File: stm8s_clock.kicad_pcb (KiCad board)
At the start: 2 copper layers, 200 x 80 mm, 157 parts, among them J1 Conn_01x04, J2 PS, Q1 BC847, Q10 BC847, Q11 BC847, Q12 BC847, Q13 BC847, Q14 BC847, Q15 BC847, Q16 BC847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

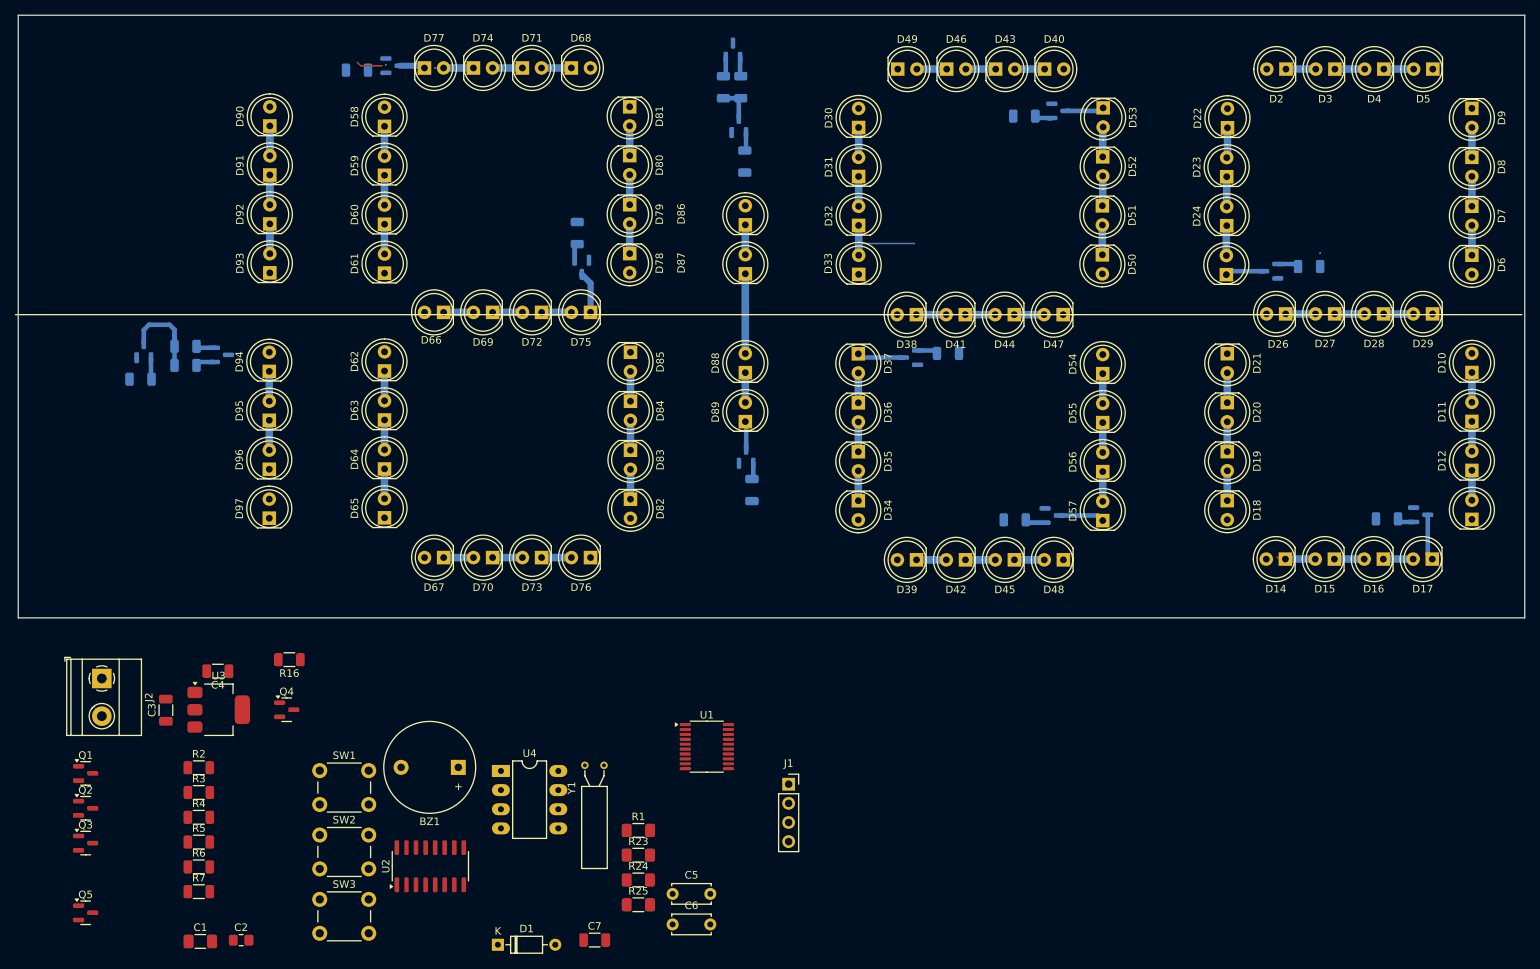
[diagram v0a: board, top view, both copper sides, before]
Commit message: move transistor to workspace
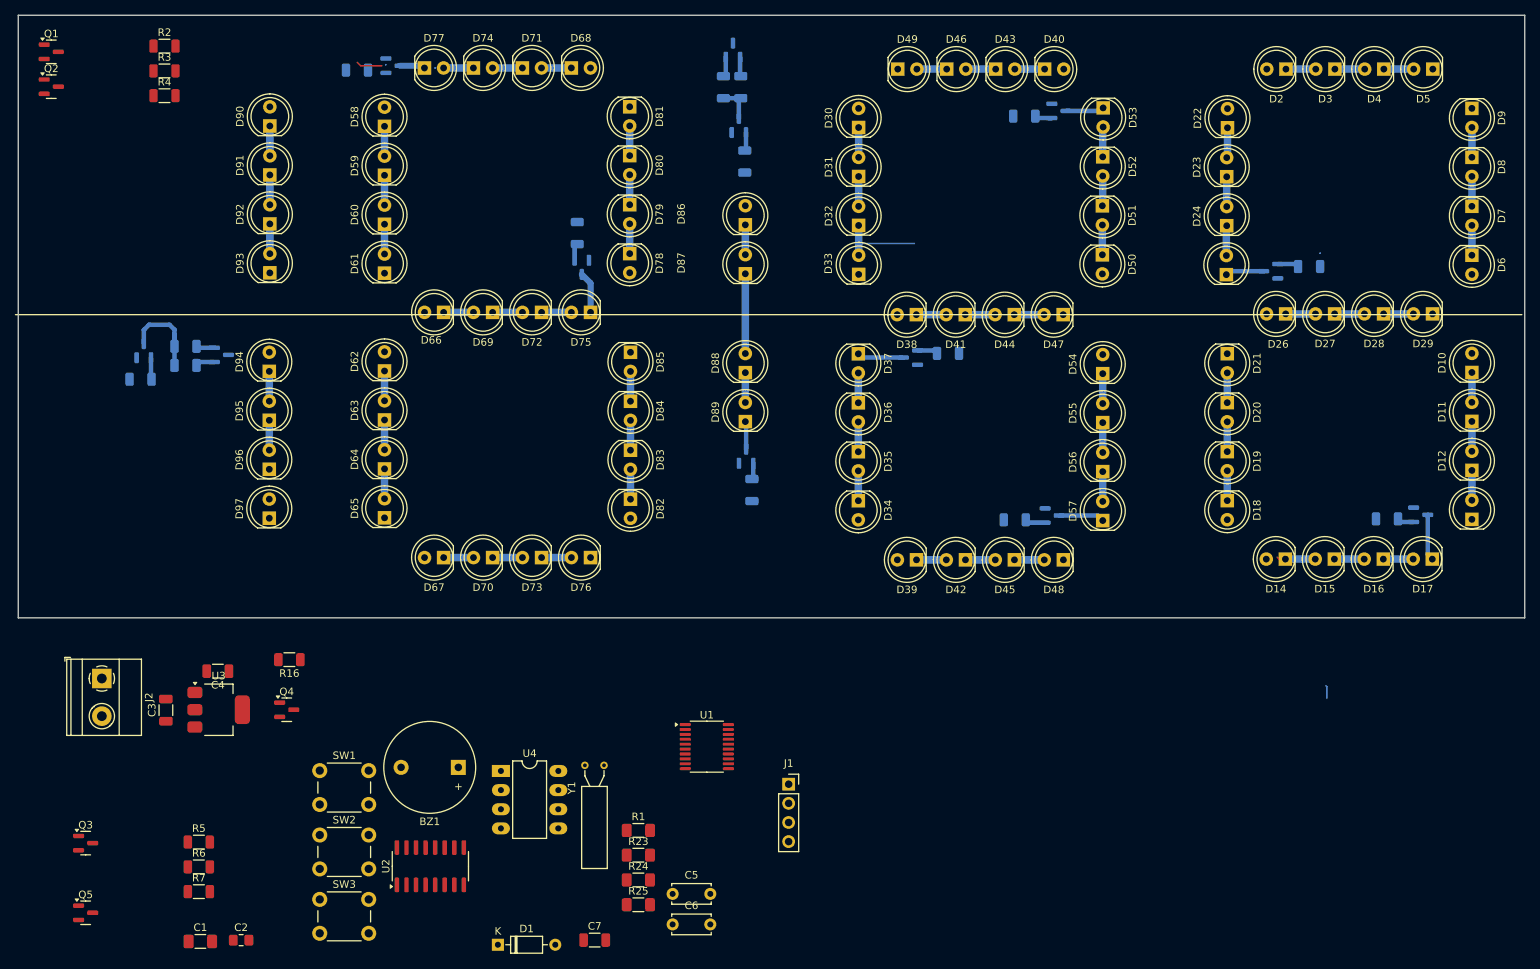
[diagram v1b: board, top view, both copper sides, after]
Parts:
- moved R4 95.9 mm to (82.2, 60.6)
- moved R2 95.9 mm to (82.2, 54.0)
- moved Q1 95.9 mm to (67.2, 54.8)
- moved Q2 95.9 mm to (67.2, 59.4)
- moved R3 95.9 mm to (82.2, 57.3)
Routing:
- net (no net): track 0.00 -> 1.74 mm
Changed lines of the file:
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@@
 	(footprint "Resistor_SMD:R_1206_3216Metric"
 		(layer "F.Cu")
-		(at 86.75 153.14)
+		(at 82.1875 57.34)
 		(descr "Resistor SMD 1206 (3216 Metric), square (rectangular) end terminal, IPC_7351 nominal, (Body size source: IPC-SM-782 page 72, https://www.pcb-3d.com/wordpress/wp-content/uploads/ipc-sm-782a_amendment_1_and_2.pdf), generated with kicad-footprint-generator")
 		(tags "resistor")
@@
 	(footprint "Package_TO_SOT_SMD:SOT-23"
 		(layer "F.Cu")
-		(at 71.72 150.605)
+		(at 67.1575 54.805)
 		(descr "SOT, 3 Pin (https://www.jedec.org/system/files/docs/to-236h.pdf variant AB), generated with kicad-footprint-generator ipc_gullwing_generator.py")
 		(tags "SOT TO_SOT_SMD")
@@
 	(footprint "Package_TO_SOT_SMD:SOT-23"
 		(layer "F.Cu")
-		(at 71.72 155.23)
+		(at 67.1575 59.43)
 		(descr "SOT, 3 Pin (https://www.jedec.org/system/files/docs/to-236h.pdf variant AB), generated with kicad-footprint-generator ipc_gullwing_generator.py")
 		(tags "SOT TO_SOT_SMD")
@@
 	(footprint "Resistor_SMD:R_1206_3216Metric"
 		(layer "F.Cu")
-		(at 86.75 156.43)
+		(at 82.1875 60.63)
 		(descr "Resistor SMD 1206 (3216 Metric), square (rectangular) end terminal, IPC_7351 nominal, (Body size source: IPC-SM-782 page 72, https://www.pcb-3d.com/wordpress/wp-content/uploads/ipc-sm-782a_amendment_1_and_2.pdf), generated with kicad-footprint-generator")
 		(tags "resistor")
@@
 		)
 		(property "Value" "LED"
-			(at 1.19 3.96 -0)
+			(at 1.19 3.96 0)
 			(layer "B.Fab")
 			(effects
@@
 	(footprint "Resistor_SMD:R_1206_3216Metric"
 		(layer "F.Cu")
-		(at 86.75 149.85)
+		(at 82.1875 54.05)
 		(descr "Resistor SMD 1206 (3216 Metric), square (rectangular) end terminal, IPC_7351 nominal, (Body size source: IPC-SM-782 page 72, https://www.pcb-3d.com/wordpress/wp-content/uploads/ipc-sm-782a_amendment_1_and_2.pdf), generated with kicad-footprint-generator")
 		(tags "resistor")
@@
 		(tags "SOT TO_SOT_SMD")
 		(property "Reference" "Q11"
-			(at 0 2.4 360)
+			(at 0 2.4 0)
 			(layer "B.SilkS")
 			(effects
@@
 		)
 		(property "Value" "BC847"
-			(at 0 -2.4 360)
+			(at 0 -2.4 0)
 			(layer "B.Fab")
 			(effects
@@
 		)
 		(fp_text user "${REFERENCE}"
-			(at 0 0 360)
+			(at 0 0 0)
 			(layer "B.Fab")
 			(effects
@@
 		(tags "resistor")
 		(property "Reference" "R13"
-			(at 0 1.82 360)
+			(at 0 1.82 0)
 			(layer "B.SilkS")
 			(effects
@@
 		)
 		(property "Value" "470R"
-			(at 0 -1.82 360)
+			(at 0 -1.82 0)
 			(layer "B.Fab")
 			(effects
@@
 		)
 		(fp_text user "${REFERENCE}"
-			(at 0 0 360)
+			(at 0 0 0)
 			(layer "B.Fab")
 			(effects
@@
 		(tags "SOT TO_SOT_SMD")
 		(property "Reference" "Q12"
-			(at 0 2.4 360)
+			(at 0 2.4 0)
 			(layer "B.SilkS")
 			(effects
@@
 		)
 		(property "Value" "BC847"
-			(at 0 -2.4 360)
+			(at 0 -2.4 0)
 			(layer "B.Fab")
 			(effects
@@
 		)
 		(fp_text user "${REFERENCE}"
-			(at 0 0 360)
+			(at 0 0 0)
 			(layer "B.Fab")
 			(effects
@@
 		(tags "SOT TO_SOT_SMD")
 		(property "Reference" "Q10"
-			(at 0 2.4 360)
+			(at 0 2.4 0)
 			(layer "B.SilkS")
 			(effects
@@
 		)
 		(property "Value" "BC847"
-			(at 0 -2.4 360)
+			(at 0 -2.4 0)
 			(layer "B.Fab")
 			(effects
@@
 		)
 		(fp_text user "${REFERENCE}"
-			(at 3.51 9.235 360)
+			(at 3.51 9.235 0)
 			(layer "B.Fab")
 			(effects
@@
 		(tags "SOT TO_SOT_SMD")
 		(property "Reference" "Q9"
-			(at 0 2.4 360)
+			(at 0 2.4 0)
 			(layer "B.SilkS")
 			(effects
@@
 		)
 		(property "Value" "BC857"
-			(at 0 -2.4 360)
+			(at 0 -2.4 0)
 			(layer "B.Fab")
 			(effects
@@
 		)
 		(fp_text user "${REFERENCE}"
-			(at 0 0 360)
+			(at 0 0 0)
 			(layer "B.Fab")
 			(effects
@@
 		(tags "SOT TO_SOT_SMD")
 		(property "Reference" "Q13"
-			(at 0 2.4 360)
+			(at 0 2.4 0)
 			(layer "B.SilkS")
 			(effects
@@
 		)
 		(property "Value" "BC847"
-			(at 0 -2.4 360)
+			(at 0 -2.4 0)
 			(layer "B.Fab")
 			(effects
@@
 		)
 		(fp_text user "${REFERENCE}"
-			(at 0 0 360)
+			(at 0 0 0)
 			(layer "B.Fab")
 			(effects
@@
 		(tags "resistor")
 		(property "Reference" "R11"
-			(at 0 1.82 360)
+			(at 0 1.82 0)
 			(layer "B.SilkS")
 			(effects
@@
 		)
 		(property "Value" "4.7k"
-			(at 0 -1.82 360)
+			(at 0 -1.82 0)
 			(layer "B.Fab")
 			(effects
@@
 		)
 		(fp_text user "${REFERENCE}"
-			(at 0 0 360)
+			(at 0 0 0)
 			(layer "B.Fab")
 			(effects
@@
 		(tags "SOT TO_SOT_SMD")
 		(property "Reference" "Q15"
-			(at 0 2.4 360)
+			(at 0 2.4 0)
 			(layer "B.SilkS")
 			(effects
@@
 		)
 		(property "Value" "BC847"
-			(at 0 -2.4 360)
+			(at 0 -2.4 0)
 			(layer "B.Fab")
 			(effects
@@
 		)
 		(fp_text user "${REFERENCE}"
-			(at 0 0 360)
+			(at 0 0 0)
 			(layer "B.Fab")
 			(effects
@@
 		(tags "resistor")
 		(property "Reference" "R19"
-			(at 0 1.82 360)
+			(at 0 1.82 0)
 			(layer "B.SilkS")
 			(effects
@@
 		)
 		(property "Value" "1k"
-			(at 0 -1.82 360)
+			(at 0 -1.82 0)
 			(layer "B.Fab")
 			(effects
@@
 		)
 		(fp_text user "${REFERENCE}"
-			(at 0 0 360)
+			(at 0 0 0)
 			(layer "B.Fab")
 			(effects
@@
 		(tags "resistor")
 		(property "Reference" "R14"
-			(at 0 1.82 360)
+			(at 0 1.82 0)
 			(layer "B.SilkS")
 			(effects
@@
 		)
 		(property "Value" "1k"
-			(at 0 -1.82 360)
+			(at 0 -1.82 0)
 			(layer "B.Fab")
 			(effects
@@
 		)
 		(fp_text user "${REFERENCE}"
-			(at 0 0 360)
+			(at 0 0 0)
 			(layer "B.Fab")
 			(effects
@@
 		(tags "resistor")
 		(property "Reference" "R15"
-			(at 0 1.82 360)
+			(at 0 1.82 0)
 			(layer "B.SilkS")
 			(effects
@@
 		)
 		(property "Value" "470R"
-			(at 0 -1.82 360)
+			(at 0 -1.82 0)
 			(layer "B.Fab")
 			(effects
@@
 		)
 		(fp_text user "${REFERENCE}"
-			(at 0 0 360)
+			(at 0 0 0)
 			(layer "B.Fab")
 			(effects
@@
 		(tags "resistor")
 		(property "Reference" "R20"
-			(at 0 1.82 360)
+			(at 0 1.82 0)
 			(layer "B.SilkS")
 			(effects
@@
 		)
 		(property "Value" "1k"
-			(at 0 -1.82 360)
+			(at 0 -1.82 0)
 			(layer "B.Fab")
 			(effects
@@
 		)
 		(fp_text user "${REFERENCE}"
-			(at 0 0 360)
+			(at 0 0 0)
 			(layer "B.Fab")
 			(effects
@@
 		(tags "resistor")
 		(property "Reference" "R12"
-			(at 0 1.82 360)
+			(at 0 1.82 0)
 			(layer "B.SilkS")
 			(effects
@@
 		)
 		(property "Value" "4.7k"
-			(at 0 -1.82 360)
+			(at 0 -1.82 0)
 			(layer "B.Fab")
 			(effects
@@
 		)
 		(fp_text user "${REFERENCE}"
-			(at 0 0 360)
+			(at 0 0 0)
 			(layer "B.Fab")
 			(effects
@@
 		(tags "resistor")
 		(property "Reference" "R18"
-			(at 0 1.82 360)
+			(at 0 1.82 0)
 			(layer "B.SilkS")
 			(effects
@@
 		)
 		(property "Value" "1k"
-			(at 0 -1.82 360)
+			(at 0 -1.82 0)
 			(layer "B.Fab")
 			(effects
@@
 		)
 		(fp_text user "${REFERENCE}"
-			(at 0 0 360)
+			(at 0 0 0)
 			(layer "B.Fab")
 			(effects
@@
 		(tags "resistor")
 		(property "Reference" "R17"
-			(at 0 1.82 360)
+			(at 0 1.82 0)
 			(layer "B.SilkS")
 			(effects
@@
 		)
 		(property "Value" "1k"
-			(at 0 -1.82 360)
+			(at 0 -1.82 0)
 			(layer "B.Fab")
 			(effects
@@
 		)
 		(fp_text user "${REFERENCE}"
-			(at 0 0 360)
+			(at 0 0 0)
 			(layer "B.Fab")
 			(effects
@@
 		(tags "SOT TO_SOT_SMD")
 		(property "Reference" "Q14"
-			(at 0 2.4 360)
+			(at 0 2.4 0)
 			(layer "B.SilkS")
 			(effects
@@
 		)
 		(property "Value" "BC847"
-			(at 0 -2.4 360)
+			(at 0 -2.4 0)
 			(layer "B.Fab")
 			(effects
@@
 		)
 		(fp_text user "${REFERENCE}"
-			(at 0 0 360)
+			(at 0 0 0)
 			(layer "B.Fab")
 			(effects
@@
 	)
 	(segment
+		(start 236.5 140.65)
+		(end 236.5 139.09)
+		(width 0.2)
+		(layer "B.Cu")
+		(net 0)
+	)
+	(segment
+		(start 236.5 139.09)
+		(end 236.37 138.96)
+		(width 0.2)
+		(layer "B.Cu")
+		(net 0)
+	)
+	(segment

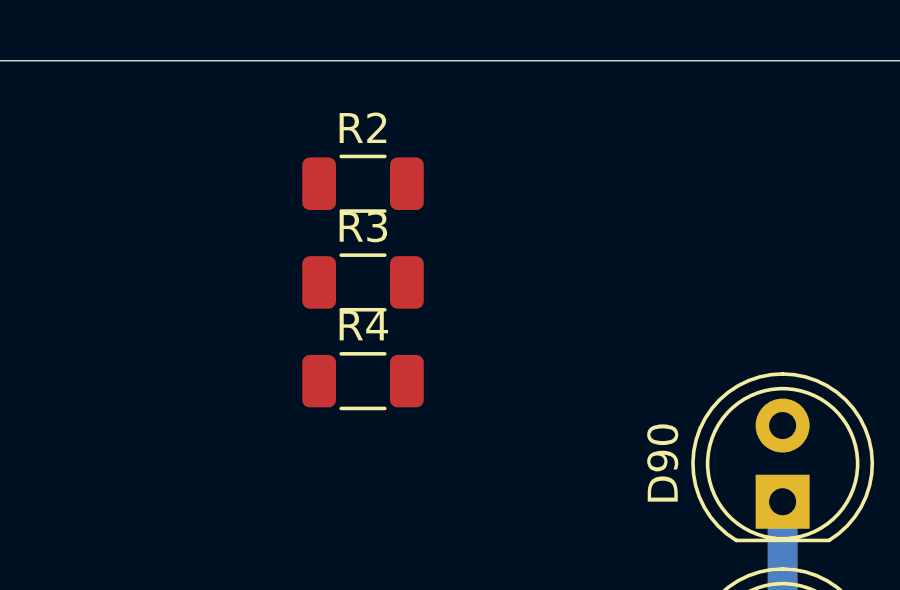
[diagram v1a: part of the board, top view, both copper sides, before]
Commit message: component position changes
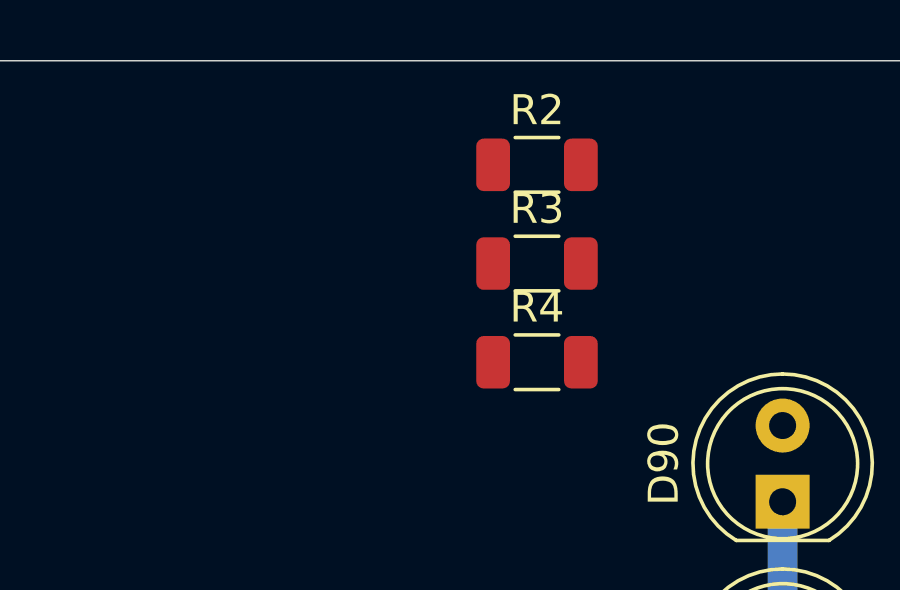
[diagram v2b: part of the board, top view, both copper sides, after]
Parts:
- moved R3 5.83 mm to (88.0, 56.7)
- moved R4 5.83 mm to (88.0, 60.0)
- moved R2 5.83 mm to (88.0, 53.4)
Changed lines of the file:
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@@
 	(footprint "Resistor_SMD:R_1206_3216Metric"
 		(layer "F.Cu")
-		(at 82.1875 57.34)
+		(at 87.9875 56.71)
 		(descr "Resistor SMD 1206 (3216 Metric), square (rectangular) end terminal, IPC_7351 nominal, (Body size source: IPC-SM-782 page 72, https://www.pcb-3d.com/wordpress/wp-content/uploads/ipc-sm-782a_amendment_1_and_2.pdf), generated with kicad-footprint-generator")
 		(tags "resistor")
@@
 	(footprint "Resistor_SMD:R_1206_3216Metric"
 		(layer "F.Cu")
-		(at 82.1875 60.63)
+		(at 87.9875 60)
 		(descr "Resistor SMD 1206 (3216 Metric), square (rectangular) end terminal, IPC_7351 nominal, (Body size source: IPC-SM-782 page 72, https://www.pcb-3d.com/wordpress/wp-content/uploads/ipc-sm-782a_amendment_1_and_2.pdf), generated with kicad-footprint-generator")
 		(tags "resistor")
@@
 	(footprint "Resistor_SMD:R_1206_3216Metric"
 		(layer "F.Cu")
-		(at 82.1875 54.05)
+		(at 87.9875 53.42)
 		(descr "Resistor SMD 1206 (3216 Metric), square (rectangular) end terminal, IPC_7351 nominal, (Body size source: IPC-SM-782 page 72, https://www.pcb-3d.com/wordpress/wp-content/uploads/ipc-sm-782a_amendment_1_and_2.pdf), generated with kicad-footprint-generator")
 		(tags "resistor")
